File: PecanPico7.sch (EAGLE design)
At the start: 153 parts, among them IC1 Si4464-B1B-FM, IC10 TC1185-1.8VCT713, IC11 TC1185-2.5VCT713, IC12 ADR380ARTZ, IC13 RF6886, IC2 Si4464-B1B-FM, IC3 BME280_BME280, IC4 UBLOX_MAX-6, IC5 STM32F429IIH6, IC7 SPV1040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

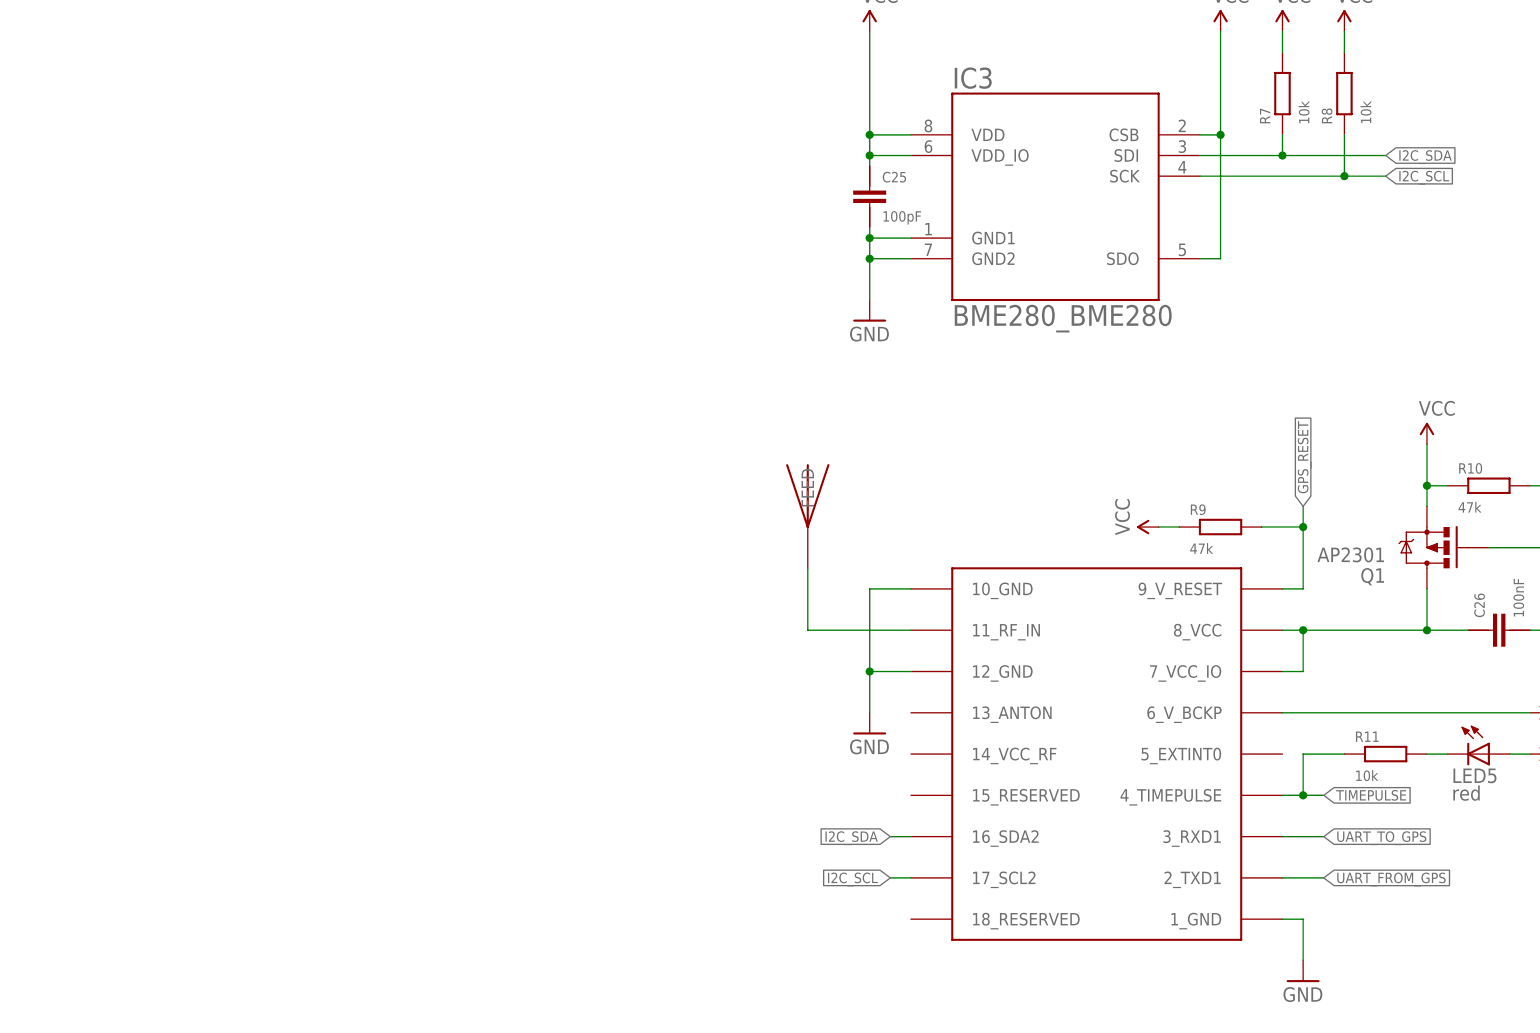
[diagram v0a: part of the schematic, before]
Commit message: Added GPS preamplifier
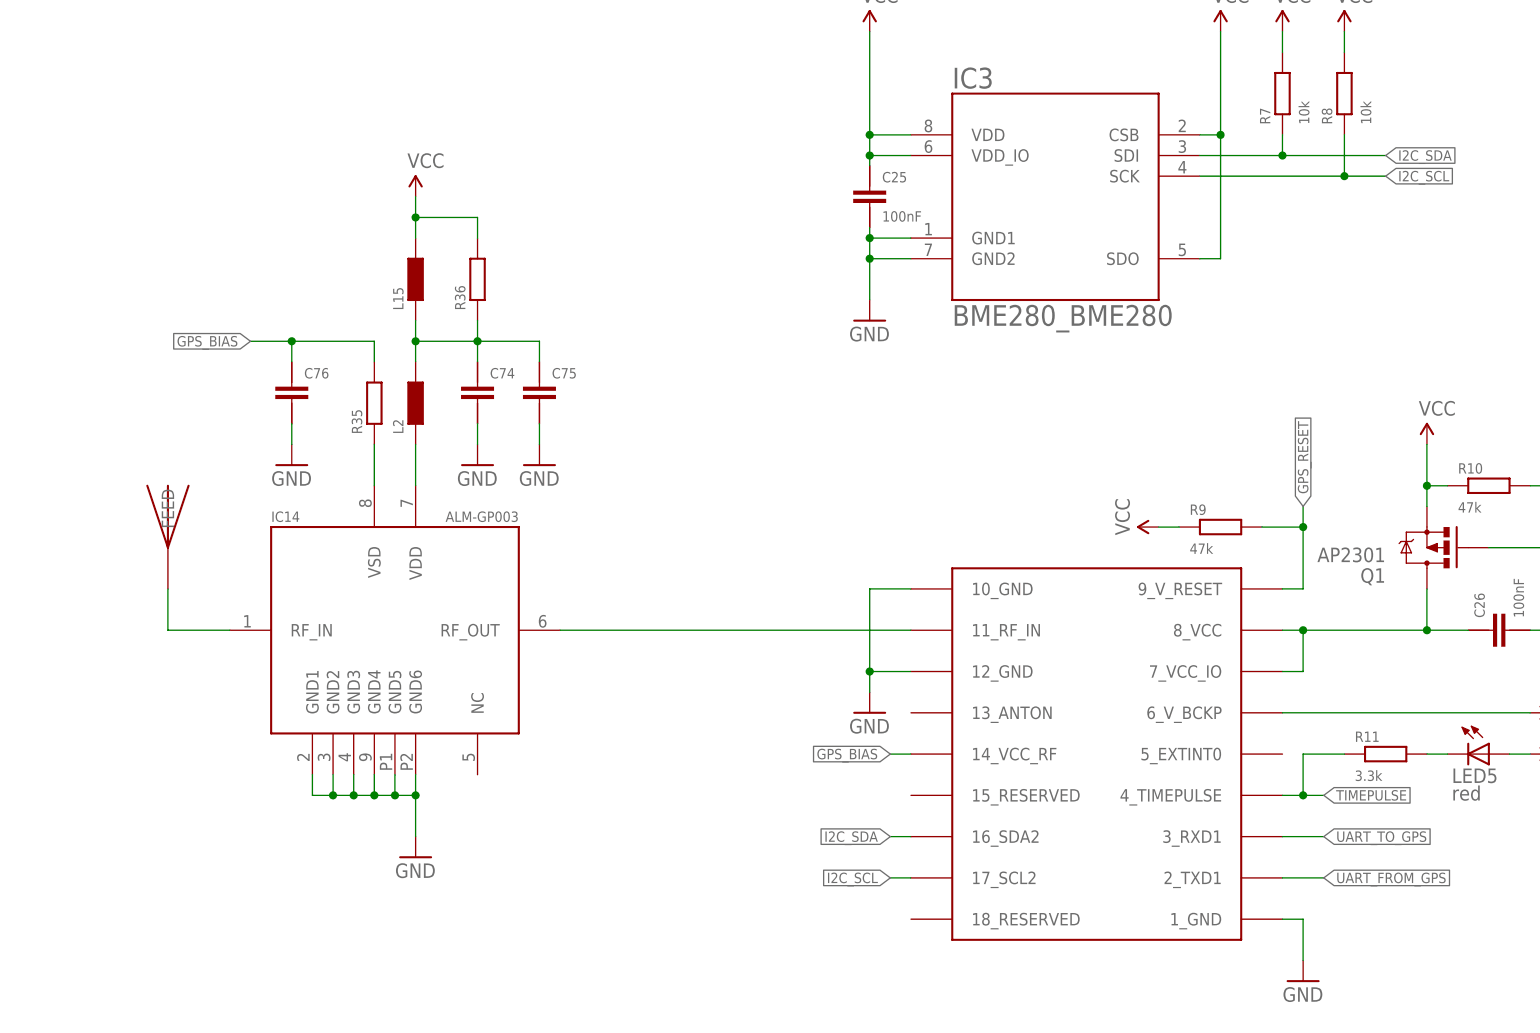
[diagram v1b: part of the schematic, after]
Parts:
- added C74, C75, C76: CAP-0402, PecanPico6:CAP-0402
- added IC14: ALM-GP003, stm32f42x:ALM-GP003
- added L15, L2: IND-0402, PecanPico6:IND-0402
- added R35, R36: RES-0402, PecanPico6:RES-0402
- C25: value 100pF -> 100nF
- R11: value 10k -> 3.3k
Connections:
- new net GPS_BIAS: C76.2, IC4.14_VCC_RF, R35.2
- new net N$45: IC14.VSD, R35.1
- new net N$46: IC14.VDD, L2.1
- new net N$51: C74.2, C75.2, L15.1, L2.2, R36.1
- new net N$7: IC14.RF_IN, U$4.FEED
- net GND: now also C74.1, C75.1, C76.1, IC14.GND1, IC14.GND2, IC14.GND3, IC14.GND4, IC14.GND5, IC14.GND6
- net N$33: now also IC14.RF_OUT; no longer U$4.FEED
- net VCC: now also L15.2, R36.2
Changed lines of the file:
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@@
 <part name="P+6" library="PecanPico6" deviceset="3.3V" device="" value="VCC"/>
 <part name="P+7" library="PecanPico6" deviceset="3.3V" device="" value="VCC"/>
-<part name="C25" library="PecanPico6" deviceset="CAP-0402" device="" value="100pF"/>
+<part name="C25" library="PecanPico6" deviceset="CAP-0402" device="" value="100nF"/>
 <part name="P+8" library="PecanPico6" deviceset="3.3V" device="" value="VCC"/>
 <part name="GND27" library="PecanPico6" deviceset="GND" device=""/>
@@
 <part name="U$4" library="PecanPico6" deviceset="JTI_ANTENNA-1575AT43A40" device=""/>
 <part name="LED5" library="PecanPico6" deviceset="LED" device="0603" value="red"/>
-<part name="R11" library="PecanPico6" deviceset="RES-0402" device="" value="10k"/>
+<part name="R11" library="PecanPico6" deviceset="RES-0402" device="" value="3.3k"/>
 <part name="P+12" library="PecanPico6" deviceset="3.3V" device="" value="VCC"/>
 <part name="IC5" library="stm32f42x" deviceset="STM32F429IIH6" device=""/>
@@
 <part name="P+38" library="PecanPico6" deviceset="3.3V" device="" value="VCC"/>
 <part name="GND95" library="PecanPico6" deviceset="GND" device=""/>
+<part name="IC14" library="stm32f42x" deviceset="ALM-GP003" device=""/>
+<part name="GND94" library="PecanPico6" deviceset="GND" device=""/>
+<part name="L2" library="PecanPico6" deviceset="IND-0402" device="" value=""/>
+<part name="L15" library="PecanPico6" deviceset="IND-0402" device="" value=""/>
+<part name="R36" library="PecanPico6" deviceset="RES-0402" device="" value=""/>
+<part name="C74" library="PecanPico6" deviceset="CAP-0402" device="" value=""/>
+<part name="C75" library="PecanPico6" deviceset="CAP-0402" device="" value=""/>
+<part name="P+37" library="PecanPico6" deviceset="3.3V" device="" value="VCC"/>
+<part name="GND96" library="PecanPico6" deviceset="GND" device=""/>
+<part name="GND97" library="PecanPico6" deviceset="GND" device=""/>
+<part name="R35" library="PecanPico6" deviceset="RES-0402" device="" value=""/>
+<part name="C76" library="PecanPico6" deviceset="CAP-0402" device="" value=""/>
+<part name="GND98" library="PecanPico6" deviceset="GND" device=""/>
 </parts>
 <sheets>
@@
 <instance part="P+11" gate="G$1" x="231.14" y="388.62" rot="R270"/>
 <instance part="GND29" gate="1" x="203.2" y="355.6"/>
-<instance part="GND30" gate="1" x="149.86" y="386.08"/>
-<instance part="U$4" gate="G$1" x="142.24" y="414.02" rot="R90"/>
+<instance part="GND30" gate="1" x="149.86" y="388.62"/>
+<instance part="U$4" gate="G$1" x="63.5" y="411.48" rot="R90"/>
 <instance part="LED5" gate="G$1" x="226.06" y="383.54" rot="R270"/>
 <instance part="R11" gate="G$1" x="213.36" y="383.54"/>
@@
 <instance part="P+38" gate="G$1" x="121.92" y="330.2"/>
 <instance part="GND95" gate="1" x="152.4" y="294.64" rot="R90"/>
+<instance part="IC14" gate="G$1" x="91.44" y="398.78"/>
+<instance part="GND94" gate="1" x="93.98" y="370.84"/>
+<instance part="L2" gate="G$1" x="93.98" y="426.72" rot="R90"/>
+<instance part="L15" gate="G$1" x="93.98" y="441.96" rot="R90"/>
+<instance part="R36" gate="G$1" x="101.6" y="441.96" rot="R90"/>
+<instance part="C74" gate="G$1" x="101.6" y="429.26"/>
+<instance part="C75" gate="G$1" x="109.22" y="429.26"/>
+<instance part="P+37" gate="G$1" x="93.98" y="452.12"/>
+<instance part="GND96" gate="1" x="101.6" y="419.1"/>
+<instance part="GND97" gate="1" x="109.22" y="419.1"/>
+<instance part="R35" gate="G$1" x="88.9" y="426.72" rot="R90"/>
+<instance part="C76" gate="G$1" x="78.74" y="429.26"/>
+<instance part="GND98" gate="1" x="78.74" y="419.1"/>
 </instances>
 <busses>
@@
 <pinref part="IC4" gate="G$1" pin="12_GND"/>
 <wire x1="154.94" y1="393.7" x2="149.86" y2="393.7" width="0.1524" layer="91"/>
-<wire x1="149.86" y1="393.7" x2="149.86" y2="388.62" width="0.1524" layer="91"/>
+<wire x1="149.86" y1="393.7" x2="149.86" y2="391.16" width="0.1524" layer="91"/>
 <wire x1="149.86" y1="393.7" x2="149.86" y2="403.86" width="0.1524" layer="91"/>
 <junction x="149.86" y="393.7"/>
@@
 <pinref part="GND95" gate="1" pin="GND"/>
 </segment>
+<segment>
+<pinref part="IC14" gate="G$1" pin="GND6"/>
+<wire x1="93.98" y1="381" x2="93.98" y2="378.46" width="0.1524" layer="91"/>
+<pinref part="IC14" gate="G$1" pin="GND5"/>
+<wire x1="91.44" y1="381" x2="91.44" y2="378.46" width="0.1524" layer="91"/>
+<wire x1="91.44" y1="378.46" x2="93.98" y2="378.46" width="0.1524" layer="91"/>
+<pinref part="IC14" gate="G$1" pin="GND4"/>
+<wire x1="88.9" y1="381" x2="88.9" y2="378.46" width="0.1524" layer="91"/>
+<wire x1="88.9" y1="378.46" x2="91.44" y2="378.46" width="0.1524" layer="91"/>
+<junction x="91.44" y="378.46"/>
+<pinref part="IC14" gate="G$1" pin="GND3"/>
+<wire x1="86.36" y1="381" x2="86.36" y2="378.46" width="0.1524" layer="91"/>
+<wire x1="86.36" y1="378.46" x2="88.9" y2="378.46" width="0.1524" layer="91"/>
+<junction x="88.9" y="378.46"/>
+<pinref part="IC14" gate="G$1" pin="GND2"/>
+<wire x1="83.82" y1="381" x2="83.82" y2="378.46" width="0.1524" layer="91"/>
+<wire x1="83.82" y1="378.46" x2="86.36" y2="378.46" width="0.1524" layer="91"/>
+<junction x="86.36" y="378.46"/>
+<pinref part="IC14" gate="G$1" pin="GND1"/>
+<wire x1="81.28" y1="381" x2="81.28" y2="378.46" width="0.1524" layer="91"/>
+<wire x1="81.28" y1="378.46" x2="83.82" y2="378.46" width="0.1524" layer="91"/>
+<junction x="83.82" y="378.46"/>
+<wire x1="93.98" y1="378.46" x2="93.98" y2="373.38" width="0.1524" layer="91"/>
+<junction x="93.98" y="378.46"/>
+<pinref part="GND94" gate="1" pin="GND"/>
+</segment>
+<segment>
+<pinref part="C74" gate="G$1" pin="1"/>
+<wire x1="101.6" y1="424.18" x2="101.6" y2="421.64" width="0.1524" layer="91"/>
+<pinref part="GND96" gate="1" pin="GND"/>
+</segment>
+<segment>
+<pinref part="C75" gate="G$1" pin="1"/>
+<wire x1="109.22" y1="424.18" x2="109.22" y2="421.64" width="0.1524" layer="91"/>
+<pinref part="GND97" gate="1" pin="GND"/>
+</segment>
+<segment>
+<pinref part="C76" gate="G$1" pin="1"/>
+<pinref part="GND98" gate="1" pin="GND"/>
+<wire x1="78.74" y1="421.64" x2="78.74" y2="424.18" width="0.1524" layer="91"/>
+</segment>
 </net>
 <net name="N$5" class="0">
@@
 <junction x="121.92" y="325.12"/>
 </segment>
+<segment>
+<pinref part="L15" gate="G$1" pin="2"/>
+<wire x1="93.98" y1="447.04" x2="93.98" y2="449.58" width="0.1524" layer="91"/>
+<pinref part="R36" gate="G$1" pin="2"/>
+<wire x1="101.6" y1="447.04" x2="101.6" y2="449.58" width="0.1524" layer="91"/>
+<wire x1="101.6" y1="449.58" x2="93.98" y2="449.58" width="0.1524" layer="91"/>
+<wire x1="93.98" y1="449.58" x2="93.98" y2="452.12" width="0.1524" layer="91"/>
+<junction x="93.98" y="449.58"/>
+<pinref part="P+37" gate="G$1" pin="VCC"/>
+</segment>
 </net>
 <net name="N$14" class="0">
@@
 <segment>
 <pinref part="IC4" gate="G$1" pin="11_RF_IN"/>
-<wire x1="154.94" y1="398.78" x2="142.24" y2="398.78" width="0.1524" layer="91"/>
-<wire x1="142.24" y1="398.78" x2="142.24" y2="406.4" width="0.1524" layer="91"/>
-<pinref part="U$4" gate="G$1" pin="FEED"/>
+<wire x1="154.94" y1="398.78" x2="111.76" y2="398.78" width="0.1524" layer="91"/>
+<pinref part="IC14" gate="G$1" pin="RF_OUT"/>
 </segment>
 </net>
@@
 </segment>
 </net>
+<net name="N$7" class="0">
+<segment>
+<pinref part="U$4" gate="G$1" pin="FEED"/>
+<pinref part="IC14" gate="G$1" pin="RF_IN"/>
+<wire x1="63.5" y1="403.86" x2="63.5" y2="398.78" width="0.1524" layer="91"/>
+<wire x1="63.5" y1="398.78" x2="71.12" y2="398.78" width="0.1524" layer="91"/>
+</segment>
+</net>
+<net name="GPS_BIAS" class="0">
+<segment>
+<pinref part="IC4" gate="G$1" pin="14_VCC_RF"/>
+<wire x1="154.94" y1="383.54" x2="152.4" y2="383.54" width="0.1524" layer="91"/>
+<label x="152.4" y="383.54" size="1.27" layer="95" rot="R180" xref="yes"/>
+</segment>
+<segment>
+<pinref part="C76" gate="G$1" pin="2"/>
+<wire x1="78.74" y1="431.8" x2="78.74" y2="434.34" width="0.1524" layer="91"/>
+<wire x1="78.74" y1="434.34" x2="88.9" y2="434.34" width="0.1524" layer="91"/>
+<pinref part="R35" gate="G$1" pin="2"/>
+<wire x1="88.9" y1="434.34" x2="88.9" y2="431.8" width="0.1524" layer="91"/>
+<wire x1="78.74" y1="434.34" x2="73.66" y2="434.34" width="0.1524" layer="91"/>
+<junction x="78.74" y="434.34"/>
+<label x="73.66" y="434.34" size="1.27" layer="95" rot="R180" xref="yes"/>
+</segment>
+</net>
+<net name="N$46" class="0">
+<segment>
+<pinref part="IC14" gate="G$1" pin="VDD"/>
+<pinref part="L2" gate="G$1" pin="1"/>
+<wire x1="93.98" y1="416.56" x2="93.98" y2="421.64" width="0.1524" layer="91"/>
+</segment>
+</net>
+<net name="N$51" class="0">
+<segment>
+<pinref part="L2" gate="G$1" pin="2"/>
+<pinref part="L15" gate="G$1" pin="1"/>
+<wire x1="93.98" y1="431.8" x2="93.98" y2="434.34" width="0.1524" layer="91"/>
+<pinref part="R36" gate="G$1" pin="1"/>
+<wire x1="93.98" y1="434.34" x2="93.98" y2="436.88" width="0.1524" layer="91"/>
+<wire x1="101.6" y1="436.88" x2="101.6" y2="434.34" width="0.1524" layer="91"/>
+<wire x1="101.6" y1="434.34" x2="93.98" y2="434.34" width="0.1524" layer="91"/>
+<junction x="93.98" y="434.34"/>
+<pinref part="C74" gate="G$1" pin="2"/>
+<wire x1="101.6" y1="431.8" x2="101.6" y2="434.34" width="0.1524" layer="91"/>
+<junction x="101.6" y="434.34"/>
+<wire x1="101.6" y1="434.34" x2="109.22" y2="434.34" width="0.1524" layer="91"/>
+<pinref part="C75" gate="G$1" pin="2"/>
+<wire x1="109.22" y1="434.34" x2="109.22" y2="431.8" width="0.1524" layer="91"/>
+</segment>
+</net>
+<net name="N$45" class="0">
+<segment>
+<pinref part="IC14" gate="G$1" pin="VSD"/>
+<wire x1="88.9" y1="416.56" x2="88.9" y2="421.64" width="0.1524" layer="91"/>
+<pinref part="R35" gate="G$1" pin="1"/>
+</segment>
+</net>
